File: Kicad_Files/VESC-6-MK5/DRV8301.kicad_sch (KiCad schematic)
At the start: 45 parts, among them Q7 DMN62D0UW-7, U14 MC74VHC1GT66DF1G, U15 MC74VHC1GT66DF1G, U16 MC74VHC1GT66DF1G, U3 DRV8301DCA, U8 TC2117-3.3VEBTR

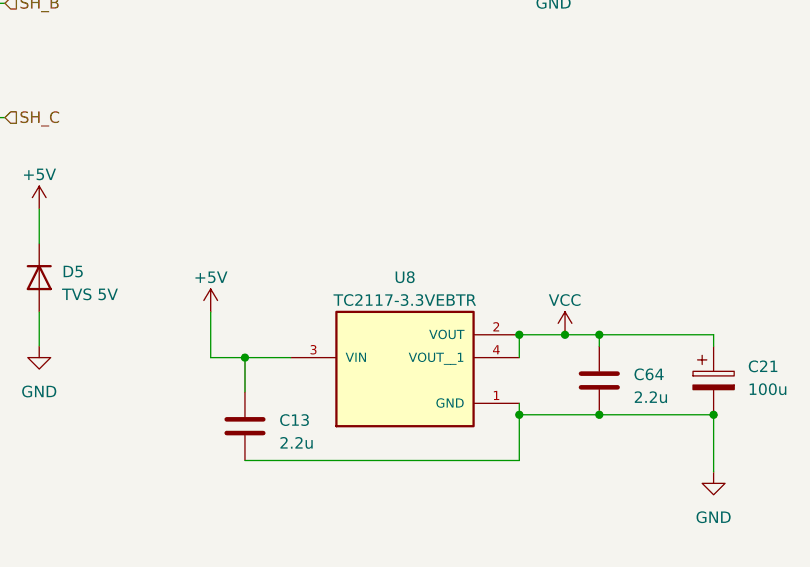
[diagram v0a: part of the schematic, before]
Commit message: Moved current sense amplifiers next to the shunt resistors
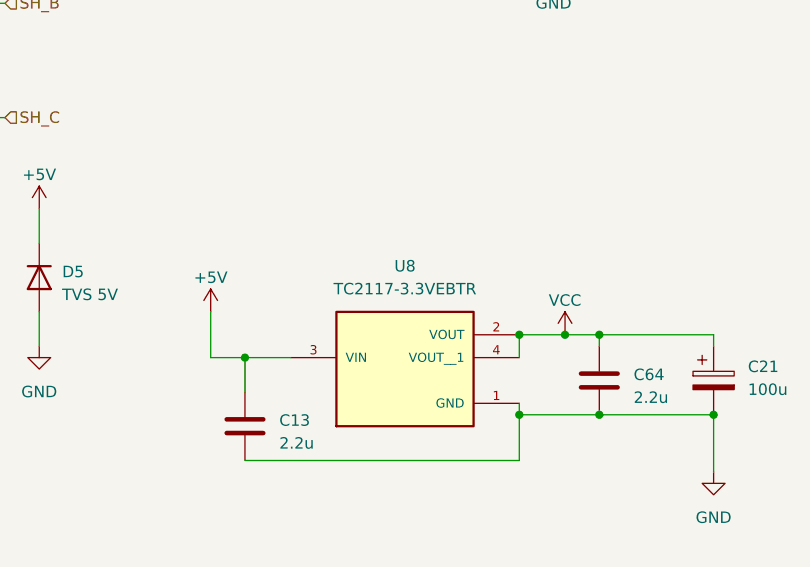
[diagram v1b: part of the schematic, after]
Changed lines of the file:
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@@
   (symbol (lib_id "TC2117-3.3VEBTR:TC2117-3.3VEBTR") (at 238.76 120.65 0) (unit 1)
     (in_bom yes) (on_board yes) (dnp no) (fields_autoplaced)
-    (property "Reference" "U8" (at 238.76 111.76 0)
+    (property "Reference" "U8" (at 238.76 110.49 0)
       (effects (font (size 1.27 1.27)))
     )
-    (property "Value" "TC2117-3.3VEBTR" (at 238.76 114.3 0)
+    (property "Value" "TC2117-3.3VEBTR" (at 238.76 113.03 0)
       (effects (font (size 1.27 1.27)))
     )
